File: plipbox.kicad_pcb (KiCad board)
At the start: 2 copper layers, 10 parts, among them P1 PWR, P2 PARALLEL_PORT, P3 RS232, U1 MAX3221, U2 ARDUINO_NANO_V3

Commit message: Routing
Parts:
- moved C2 5.93 mm to (181.2, 120.2), turned to 180 degrees
- moved P3 3.43 mm to (172.5, 120.5), turned to 180 degrees
- moved P1 2.12 mm to (172.5, 104.0)
- moved C3 1.68 mm to (181.2, 107.5), turned to 0 degrees
- moved C1 1.46 mm to (181.2, 109.8), turned to 180 degrees
- moved C4 0.56 mm to (178.2, 108.5)
- moved C5 0.25 mm to (176.0, 114.8)
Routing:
- net Net-(C4-Pad1): track 0.00 -> 5.49 mm
- net Net-(C4-Pad2): track 0.00 -> 2.92 mm
- net Net-(C1-Pad1): track 0.00 -> 2.54 mm
- net Net-(C1-Pad2): track 0.00 -> 2.31 mm
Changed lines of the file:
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@@
     (thickness 1.6)
     (drawings 1)
-    (tracks 67)
+    (tracks 79)
     (zones 0)
     (modules 10)
@@
   )
   (setup
-    (last_trace_width 0.3)
+    (last_trace_width 0.25)
     (user_trace_width 0.3)
     (user_trace_width 0.5)
@@
   )
   (module Capacitors_SMD:C_0603_HandSoldering (layer F.Cu)
-    (at 180 109 90)
+    (at 181.25 109.75 180)
     (descr "Capacitor SMD 0603, hand soldering")
     (tags "capacitor 0603")
     (attr smd)
-    (fp_text reference C1 (at 0 -1.25 90) (layer F.SilkS)
-      (effects (font (size 1 1) (thickness 0.15)))
-    )
-    (fp_text value 47n (at 0 1.5 90) (layer F.Fab)
-      (effects (font (size 1 1) (thickness 0.15)))
-    )
-    (fp_text user %R (at 0 -1.25 90) (layer F.Fab)
+    (fp_text reference C1 (at 0 -1.25 180) (layer F.SilkS)
+      (effects (font (size 1 1) (thickness 0.15)))
+    )
+    (fp_text value 47n (at 0 1.5 180) (layer F.Fab)
+      (effects (font (size 1 1) (thickness 0.15)))
+    )
+    (fp_text user %R (at 0 -1.25 180) (layer F.Fab)
       (effects (font (size 1 1) (thickness 0.15)))
     )
@@
     (fp_line (start 1.8 0.65) (end 1.8 -0.65) (layer F.CrtYd) (width 0.05))
     (fp_line (start 1.8 0.65) (end -1.8 0.65) (layer F.CrtYd) (width 0.05))
-    (pad 1 smd rect (at -0.95 0 90) (size 1.2 0.75) (layers F.Cu F.Paste F.Mask)
+    (pad 1 smd rect (at -0.95 0 180) (size 1.2 0.75) (layers F.Cu F.Paste F.Mask)
       (net 1 "Net-(C1-Pad1)"))
-    (pad 2 smd rect (at 0.95 0 90) (size 1.2 0.75) (layers F.Cu F.Paste F.Mask)
+    (pad 2 smd rect (at 0.95 0 180) (size 1.2 0.75) (layers F.Cu F.Paste F.Mask)
       (net 2 "Net-(C1-Pad2)"))
     (model Capacitors_SMD.3dshapes/C_0603.wrl
@@
   )
   (module Capacitors_SMD:C_0603_HandSoldering (layer F.Cu)
-    (at 184 115 90)
+    (at 181.25 120.25 180)
     (descr "Capacitor SMD 0603, hand soldering")
     (tags "capacitor 0603")
     (attr smd)
-    (fp_text reference C2 (at 0 -1.25 90) (layer F.SilkS)
-      (effects (font (size 1 1) (thickness 0.15)))
-    )
-    (fp_text value 100n (at 0 1.5 90) (layer F.Fab)
-      (effects (font (size 1 1) (thickness 0.15)))
-    )
-    (fp_text user %R (at 0 -1.25 90) (layer F.Fab)
+    (fp_text reference C2 (at 0 -1.25 180) (layer F.SilkS)
+      (effects (font (size 1 1) (thickness 0.15)))
+    )
+    (fp_text value 100n (at 0 1.5 180) (layer F.Fab)
+      (effects (font (size 1 1) (thickness 0.15)))
+    )
+    (fp_text user %R (at 0 -1.25 180) (layer F.Fab)
       (effects (font (size 1 1) (thickness 0.15)))
     )
@@
     (fp_line (start 1.8 0.65) (end 1.8 -0.65) (layer F.CrtYd) (width 0.05))
     (fp_line (start 1.8 0.65) (end -1.8 0.65) (layer F.CrtYd) (width 0.05))
-    (pad 1 smd rect (at -0.95 0 90) (size 1.2 0.75) (layers F.Cu F.Paste F.Mask)
+    (pad 1 smd rect (at -0.95 0 180) (size 1.2 0.75) (layers F.Cu F.Paste F.Mask)
       (net 3 /+5V))
-    (pad 2 smd rect (at 0.95 0 90) (size 1.2 0.75) (layers F.Cu F.Paste F.Mask)
+    (pad 2 smd rect (at 0.95 0 180) (size 1.2 0.75) (layers F.Cu F.Paste F.Mask)
       (net 4 GND))
     (model Capacitors_SMD.3dshapes/C_0603.wrl
@@
   )
   (module Capacitors_SMD:C_0603_HandSoldering (layer F.Cu)
-    (at 182 109 90)
+    (at 181.25 107.5)
     (descr "Capacitor SMD 0603, hand soldering")
     (tags "capacitor 0603")
     (attr smd)
-    (fp_text reference C3 (at 0 -1.25 90) (layer F.SilkS)
-      (effects (font (size 1 1) (thickness 0.15)))
-    )
-    (fp_text value 330n (at 0 1.5 90) (layer F.Fab)
-      (effects (font (size 1 1) (thickness 0.15)))
-    )
-    (fp_text user %R (at 0 -1.25 90) (layer F.Fab)
+    (fp_text reference C3 (at 0 -1.25) (layer F.SilkS)
+      (effects (font (size 1 1) (thickness 0.15)))
+    )
+    (fp_text value 330n (at 0 1.5) (layer F.Fab)
+      (effects (font (size 1 1) (thickness 0.15)))
+    )
+    (fp_text user %R (at 0 -1.25) (layer F.Fab)
       (effects (font (size 1 1) (thickness 0.15)))
     )
@@
     (fp_line (start 1.8 0.65) (end 1.8 -0.65) (layer F.CrtYd) (width 0.05))
     (fp_line (start 1.8 0.65) (end -1.8 0.65) (layer F.CrtYd) (width 0.05))
-    (pad 1 smd rect (at -0.95 0 90) (size 1.2 0.75) (layers F.Cu F.Paste F.Mask)
+    (pad 1 smd rect (at -0.95 0) (size 1.2 0.75) (layers F.Cu F.Paste F.Mask)
       (net 5 "Net-(C3-Pad1)"))
-    (pad 2 smd rect (at 0.95 0 90) (size 1.2 0.75) (layers F.Cu F.Paste F.Mask)
+    (pad 2 smd rect (at 0.95 0) (size 1.2 0.75) (layers F.Cu F.Paste F.Mask)
       (net 4 GND))
     (model Capacitors_SMD.3dshapes/C_0603.wrl
@@
   )
   (module Capacitors_SMD:C_0603_HandSoldering (layer F.Cu)
-    (at 178 109 270)
+    (at 178.25 108.5 270)
     (descr "Capacitor SMD 0603, hand soldering")
     (tags "capacitor 0603")
@@
   )
   (module Capacitors_SMD:C_0603_HandSoldering (layer F.Cu)
-    (at 176 115 270)
+    (at 176 114.75 270)
     (descr "Capacitor SMD 0603, hand soldering")
     (tags "capacitor 0603")
@@
   )
   (module Pin_Headers:Pin_Header_Straight_1x03_Pitch2.54mm (layer F.Cu)
-    (at 171 105.46)
+    (at 172.5 103.96)
     (descr "Through hole straight pin header, 1x03, 2.54mm pitch, single row")
     (tags "Through hole pin header THT 1x03 2.54mm single row")
@@
   )
   (module Pin_Headers:Pin_Header_Straight_1x03_Pitch2.54mm (layer F.Cu)
-    (at 171 117.46)
+    (at 172.5 120.54 180)
     (descr "Through hole straight pin header, 1x03, 2.54mm pitch, single row")
     (tags "Through hole pin header THT 1x03 2.54mm single row")
-    (fp_text reference P3 (at 0 -2.33) (layer F.SilkS)
-      (effects (font (size 1 1) (thickness 0.15)))
-    )
-    (fp_text value RS232 (at 0 7.41) (layer F.Fab)
+    (fp_text reference P3 (at 0 -2.33 180) (layer F.SilkS)
+      (effects (font (size 1 1) (thickness 0.15)))
+    )
+    (fp_text value RS232 (at 0 7.41 180) (layer F.Fab)
       (effects (font (size 1 1) (thickness 0.15)))
     )
@@
     (fp_line (start 1.8 6.85) (end 1.8 -1.8) (layer F.CrtYd) (width 0.05))
     (fp_line (start 1.8 -1.8) (end -1.8 -1.8) (layer F.CrtYd) (width 0.05))
-    (fp_text user %R (at 0 -2.33) (layer F.Fab)
-      (effects (font (size 1 1) (thickness 0.15)))
-    )
-    (pad 1 thru_hole rect (at 0 0) (size 1.7 1.7) (drill 1) (layers *.Cu *.Mask)
+    (fp_text user %R (at 0 -2.33 180) (layer F.Fab)
+      (effects (font (size 1 1) (thickness 0.15)))
+    )
+    (pad 1 thru_hole rect (at 0 0 180) (size 1.7 1.7) (drill 1) (layers *.Cu *.Mask)
       (net 23 /DOUT))
-    (pad 2 thru_hole oval (at 0 2.54) (size 1.7 1.7) (drill 1) (layers *.Cu *.Mask)
+    (pad 2 thru_hole oval (at 0 2.54 180) (size 1.7 1.7) (drill 1) (layers *.Cu *.Mask)
       (net 24 /RIN))
-    (pad 3 thru_hole oval (at 0 5.08) (size 1.7 1.7) (drill 1) (layers *.Cu *.Mask)
+    (pad 3 thru_hole oval (at 0 5.08 180) (size 1.7 1.7) (drill 1) (layers *.Cu *.Mask)
       (net 4 GND))
     (model ${KISYS3DMOD}/Pin_Headers.3dshapes/Pin_Header_Straight_1x03_Pitch2.54mm.wrl
@@
     (arrow2b (pts (xy 245 80) (xy 245.586421 81.126504)))
   )
+  (segment (start 181.625 112.05) (end 181.625 110.325) (width 0.3) (layer F.Cu) (net 1))
+  (segment (start 181.625 110.325) (end 182.2 109.75) (width 0.3) (layer F.Cu) (net 1))
+  (segment (start 180.325 112.05) (end 180.325 109.775) (width 0.3) (layer F.Cu) (net 2))
+  (segment (start 180.325 109.775) (end 180.3 109.75) (width 0.3) (layer F.Cu) (net 2))
+  (segment (start 179.25 110.5) (end 179.675 110.925) (width 0.3) (layer F.Cu) (net 6))
+  (segment (start 179.675 110.925) (end 179.675 112.05) (width 0.3) (layer F.Cu) (net 6))
+  (segment (start 179.25 107.875) (end 179.25 110.5) (width 0.3) (layer F.Cu) (net 6))
+  (segment (start 178.25 107.55) (end 178.925 107.55) (width 0.3) (layer F.Cu) (net 6))
+  (segment (start 178.925 107.55) (end 179.25 107.875) (width 0.3) (layer F.Cu) (net 6))
+  (segment (start 178.25 109.45) (end 178.25 110.35) (width 0.3) (layer F.Cu) (net 7))
+  (segment (start 178.25 110.35) (end 179.025 111.125) (width 0.3) (layer F.Cu) (net 7))
+  (segment (start 179.025 111.125) (end 179.025 112.05) (width 0.3) (layer F.Cu) (net 7))
   (segment (start 214.235 97.84) (end 214.235 99.042081) (width 0.3) (layer F.Cu) (net 10))
   (segment (start 216.5 123) (end 201.82 123) (width 0.3) (layer F.Cu) (net 10))

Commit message: Board outline
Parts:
- moved C3 6.39 mm to (184.5, 113.0), turned to 90 degrees
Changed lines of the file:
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@@
     (area 0 0 0 0)
     (thickness 1.6)
-    (drawings 1)
+    (drawings 10)
     (tracks 79)
     (zones 0)
@@
     (pad_to_mask_clearance 0.2)
     (aux_axis_origin 0 0)
-    (visible_elements FFFFFF7F)
+    (visible_elements FFFEFF7F)
     (pcbplotparams
       (layerselection 0x00030_80000001)
@@
   )
   (module Capacitors_SMD:C_0603_HandSoldering (layer F.Cu)
-    (at 181.25 107.5)
+    (at 184.5 113 90)
     (descr "Capacitor SMD 0603, hand soldering")
     (tags "capacitor 0603")
     (attr smd)
-    (fp_text reference C3 (at 0 -1.25) (layer F.SilkS)
-      (effects (font (size 1 1) (thickness 0.15)))
-    )
-    (fp_text value 330n (at 0 1.5) (layer F.Fab)
-      (effects (font (size 1 1) (thickness 0.15)))
-    )
-    (fp_text user %R (at 0 -1.25) (layer F.Fab)
+    (fp_text reference C3 (at 0 -1.25 90) (layer F.SilkS)
+      (effects (font (size 1 1) (thickness 0.15)))
+    )
+    (fp_text value 330n (at 0 1.5 90) (layer F.Fab)
+      (effects (font (size 1 1) (thickness 0.15)))
+    )
+    (fp_text user %R (at 0 -1.25 90) (layer F.Fab)
       (effects (font (size 1 1) (thickness 0.15)))
     )
@@
     (fp_line (start 1.8 0.65) (end 1.8 -0.65) (layer F.CrtYd) (width 0.05))
     (fp_line (start 1.8 0.65) (end -1.8 0.65) (layer F.CrtYd) (width 0.05))
-    (pad 1 smd rect (at -0.95 0) (size 1.2 0.75) (layers F.Cu F.Paste F.Mask)
+    (pad 1 smd rect (at -0.95 0 90) (size 1.2 0.75) (layers F.Cu F.Paste F.Mask)
       (net 5 "Net-(C3-Pad1)"))
-    (pad 2 smd rect (at 0.95 0) (size 1.2 0.75) (layers F.Cu F.Paste F.Mask)
+    (pad 2 smd rect (at 0.95 0 90) (size 1.2 0.75) (layers F.Cu F.Paste F.Mask)
       (net 4 GND))
     (model Capacitors_SMD.3dshapes/C_0603.wrl
@@
     )
   )
+  (gr_line (start 224 87.5) (end 171.5 87.5) (layer Margin) (width 0.2))
+  (gr_arc (start 224 90) (end 224 87.5) (angle 90) (layer Margin) (width 0.2))
+  (gr_arc (start 171.5 90) (end 169 90) (angle 90) (layer Margin) (width 0.2))
+  (gr_arc (start 171.5 121.5) (end 171.5 124) (angle 90) (layer Margin) (width 0.2))
+  (gr_arc (start 224 121.5) (end 226.5 121.5) (angle 90) (layer Margin) (width 0.2))
+  (dimension 59.5 (width 0.3) (layer Cmts.User)
+    (gr_text "59.500 mm" (at 197.75 129.35) (layer Cmts.User)
+      (effects (font (size 1.5 1.5) (thickness 0.3)))
+    )
+    (feature1 (pts (xy 227.5 125) (xy 227.5 130.7)))
+    (feature2 (pts (xy 168 125) (xy 168 130.7)))
+    (crossbar (pts (xy 168 128) (xy 227.5 128)))
+    (arrow1a (pts (xy 227.5 128) (xy 226.373496 128.586421)))
+    (arrow1b (pts (xy 227.5 128) (xy 226.373496 127.413579)))
+    (arrow2a (pts (xy 168 128) (xy 169.126504 128.586421)))
+    (arrow2b (pts (xy 168 128) (xy 169.126504 127.413579)))
+  )
+  (gr_line (start 226.5 90) (end 226.5 121.5) (layer Margin) (width 0.2))
+  (gr_line (start 171.5 124) (end 224 124) (layer Margin) (width 0.2))
+  (gr_line (start 169 90) (end 169 121.5) (layer Margin) (width 0.2))
   (dimension 45 (width 0.3) (layer Cmts.User)
     (gr_text "45.000 mm" (at 246.35 102.5 270) (layer Cmts.User)

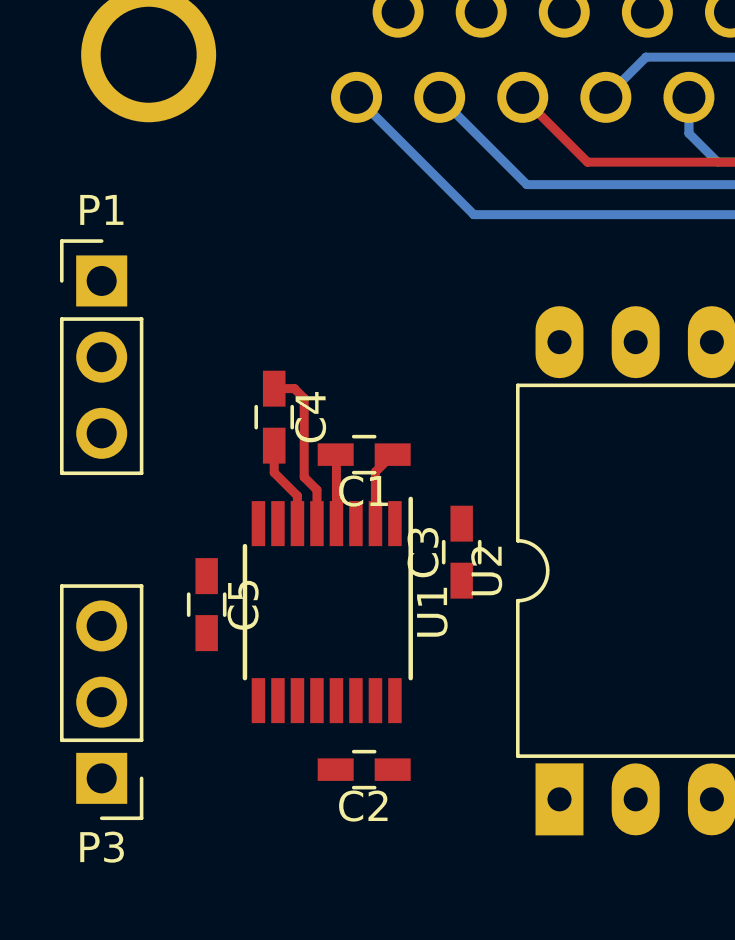
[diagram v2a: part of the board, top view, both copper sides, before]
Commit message: More compact U1
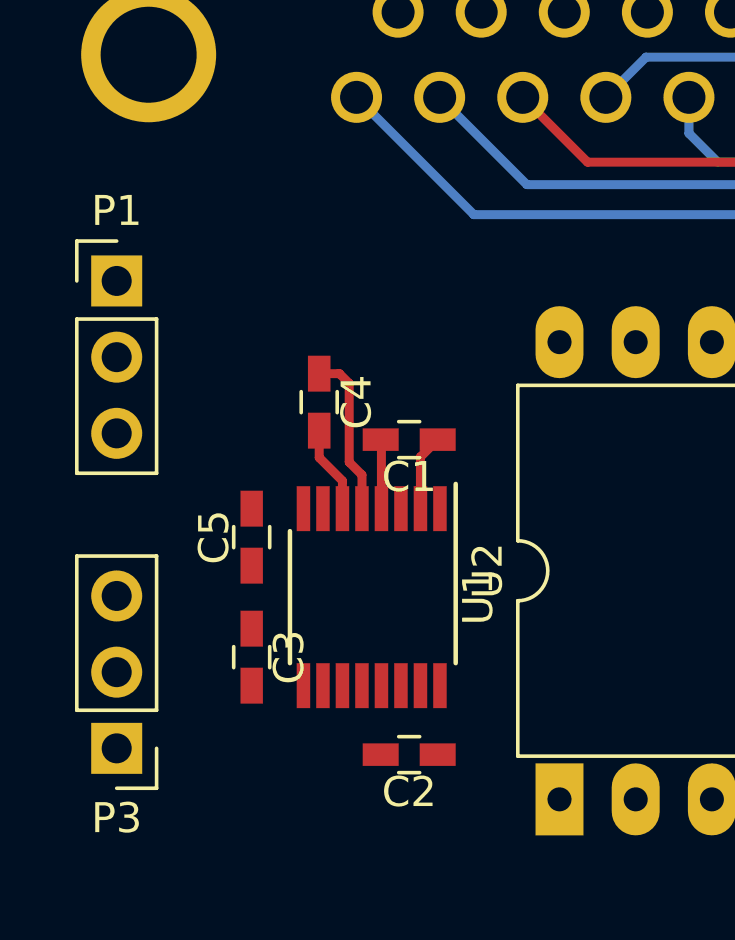
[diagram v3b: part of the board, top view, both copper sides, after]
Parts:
- moved C3 7.83 mm to (177.5, 116.5), turned to 270 degrees
- moved C5 2.70 mm to (177.5, 112.5), turned to 90 degrees
- moved C1 1.58 mm to (182.8, 109.2)
- moved C2 1.58 mm to (182.8, 119.8)
- moved C4 1.58 mm to (179.8, 108.0)
- moved U1 1.58 mm to (181.5, 114.5)
- moved P3 1.12 mm to (173.0, 119.5)
- moved P1 0.50 mm to (173.0, 104.0)
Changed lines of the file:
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@@
   )
   (setup
-    (last_trace_width 0.25)
+    (last_trace_width 0.3)
     (user_trace_width 0.3)
     (user_trace_width 0.5)
@@
   )
   (module Capacitors_SMD:C_0603_HandSoldering (layer F.Cu)
-    (at 181.25 109.75 180)
+    (at 182.75 109.25 180)
     (descr "Capacitor SMD 0603, hand soldering")
     (tags "capacitor 0603")
@@
   )
   (module Capacitors_SMD:C_0603_HandSoldering (layer F.Cu)
-    (at 181.25 120.25 180)
+    (at 182.75 119.75 180)
     (descr "Capacitor SMD 0603, hand soldering")
     (tags "capacitor 0603")
@@
   )
   (module Capacitors_SMD:C_0603_HandSoldering (layer F.Cu)
-    (at 184.5 113 90)
+    (at 177.5 116.5 270)
     (descr "Capacitor SMD 0603, hand soldering")
     (tags "capacitor 0603")
     (attr smd)
-    (fp_text reference C3 (at 0 -1.25 90) (layer F.SilkS)
-      (effects (font (size 1 1) (thickness 0.15)))
-    )
-    (fp_text value 330n (at 0 1.5 90) (layer F.Fab)
-      (effects (font (size 1 1) (thickness 0.15)))
-    )
-    (fp_text user %R (at 0 -1.25 90) (layer F.Fab)
+    (fp_text reference C3 (at 0 -1.25 270) (layer F.SilkS)
+      (effects (font (size 1 1) (thickness 0.15)))
+    )
+    (fp_text value 330n (at 0 1.5 270) (layer F.Fab)
+      (effects (font (size 1 1) (thickness 0.15)))
+    )
+    (fp_text user %R (at 0 -1.25 270) (layer F.Fab)
       (effects (font (size 1 1) (thickness 0.15)))
     )
@@
     (fp_line (start 1.8 0.65) (end 1.8 -0.65) (layer F.CrtYd) (width 0.05))
     (fp_line (start 1.8 0.65) (end -1.8 0.65) (layer F.CrtYd) (width 0.05))
-    (pad 1 smd rect (at -0.95 0 90) (size 1.2 0.75) (layers F.Cu F.Paste F.Mask)
+    (pad 1 smd rect (at -0.95 0 270) (size 1.2 0.75) (layers F.Cu F.Paste F.Mask)
       (net 5 "Net-(C3-Pad1)"))
-    (pad 2 smd rect (at 0.95 0 90) (size 1.2 0.75) (layers F.Cu F.Paste F.Mask)
+    (pad 2 smd rect (at 0.95 0 270) (size 1.2 0.75) (layers F.Cu F.Paste F.Mask)
       (net 4 GND))
     (model Capacitors_SMD.3dshapes/C_0603.wrl
@@
   )
   (module Capacitors_SMD:C_0603_HandSoldering (layer F.Cu)
-    (at 178.25 108.5 270)
+    (at 179.75 108 270)
     (descr "Capacitor SMD 0603, hand soldering")
     (tags "capacitor 0603")
@@
   )
   (module Capacitors_SMD:C_0603_HandSoldering (layer F.Cu)
-    (at 176 114.75 270)
+    (at 177.5 112.5 90)
     (descr "Capacitor SMD 0603, hand soldering")
     (tags "capacitor 0603")
     (attr smd)
-    (fp_text reference C5 (at 0 -1.25 270) (layer F.SilkS)
-      (effects (font (size 1 1) (thickness 0.15)))
-    )
-    (fp_text value 330n (at 0 1.5 270) (layer F.Fab)
-      (effects (font (size 1 1) (thickness 0.15)))
-    )
-    (fp_text user %R (at 0 -1.25 270) (layer F.Fab)
+    (fp_text reference C5 (at 0 -1.25 90) (layer F.SilkS)
+      (effects (font (size 1 1) (thickness 0.15)))
+    )
+    (fp_text value 330n (at 0 1.5 90) (layer F.Fab)
+      (effects (font (size 1 1) (thickness 0.15)))
+    )
+    (fp_text user %R (at 0 -1.25 90) (layer F.Fab)
       (effects (font (size 1 1) (thickness 0.15)))
     )
@@
     (fp_line (start 1.8 0.65) (end 1.8 -0.65) (layer F.CrtYd) (width 0.05))
     (fp_line (start 1.8 0.65) (end -1.8 0.65) (layer F.CrtYd) (width 0.05))
-    (pad 1 smd rect (at -0.95 0 270) (size 1.2 0.75) (layers F.Cu F.Paste F.Mask)
+    (pad 1 smd rect (at -0.95 0 90) (size 1.2 0.75) (layers F.Cu F.Paste F.Mask)
       (net 8 "Net-(C5-Pad1)"))
-    (pad 2 smd rect (at 0.95 0 270) (size 1.2 0.75) (layers F.Cu F.Paste F.Mask)
+    (pad 2 smd rect (at 0.95 0 90) (size 1.2 0.75) (layers F.Cu F.Paste F.Mask)
       (net 4 GND))
     (model Capacitors_SMD.3dshapes/C_0603.wrl
@@
   )
   (module Pin_Headers:Pin_Header_Straight_1x03_Pitch2.54mm (layer F.Cu)
-    (at 172.5 103.96)
+    (at 173 103.96)
     (descr "Through hole straight pin header, 1x03, 2.54mm pitch, single row")
     (tags "Through hole pin header THT 1x03 2.54mm single row")
@@
   )
   (module Pin_Headers:Pin_Header_Straight_1x03_Pitch2.54mm (layer F.Cu)
-    (at 172.5 120.54 180)
+    (at 173 119.54 180)
     (descr "Through hole straight pin header, 1x03, 2.54mm pitch, single row")
     (tags "Through hole pin header THT 1x03 2.54mm single row")
@@
   )
   (module Housings_SSOP:TSSOP-16_4.4x5mm_Pitch0.65mm (layer F.Cu)
-    (at 180 115 270)
+    (at 181.5 114.5 270)
     (descr "16-Lead Plastic Thin Shrink Small Outline (ST)-4.4 mm Body [TSSOP] (see Microchip Packaging Specification 00000049BS.pdf)")
     (tags "SSOP 0.65")
@@
     (arrow2b (pts (xy 245 80) (xy 245.586421 81.126504)))
   )
-  (segment (start 181.625 112.05) (end 181.625 110.325) (width 0.3) (layer F.Cu) (net 1))
-  (segment (start 181.625 110.325) (end 182.2 109.75) (width 0.3) (layer F.Cu) (net 1))
-  (segment (start 180.325 112.05) (end 180.325 109.775) (width 0.3) (layer F.Cu) (net 2))
-  (segment (start 180.325 109.775) (end 180.3 109.75) (width 0.3) (layer F.Cu) (net 2))
-  (segment (start 179.25 110.5) (end 179.675 110.925) (width 0.3) (layer F.Cu) (net 6))
-  (segment (start 179.675 110.925) (end 179.675 112.05) (width 0.3) (layer F.Cu) (net 6))
-  (segment (start 179.25 107.875) (end 179.25 110.5) (width 0.3) (layer F.Cu) (net 6))
-  (segment (start 178.25 107.55) (end 178.925 107.55) (width 0.3) (layer F.Cu) (net 6))
-  (segment (start 178.925 107.55) (end 179.25 107.875) (width 0.3) (layer F.Cu) (net 6))
-  (segment (start 178.25 109.45) (end 178.25 110.35) (width 0.3) (layer F.Cu) (net 7))
-  (segment (start 178.25 110.35) (end 179.025 111.125) (width 0.3) (layer F.Cu) (net 7))
-  (segment (start 179.025 111.125) (end 179.025 112.05) (width 0.3) (layer F.Cu) (net 7))
+  (segment (start 183.125 111.55) (end 183.125 109.825) (width 0.3) (layer F.Cu) (net 1))
+  (segment (start 183.125 109.825) (end 183.7 109.25) (width 0.3) (layer F.Cu) (net 1))
+  (segment (start 181.825 111.55) (end 181.825 109.275) (width 0.3) (layer F.Cu) (net 2))
+  (segment (start 181.825 109.275) (end 181.8 109.25) (width 0.3) (layer F.Cu) (net 2))
+  (segment (start 180.75 110) (end 181.175 110.425) (width 0.3) (layer F.Cu) (net 6))
+  (segment (start 181.175 110.425) (end 181.175 111.55) (width 0.3) (layer F.Cu) (net 6))
+  (segment (start 180.75 107.375) (end 180.75 110) (width 0.3) (layer F.Cu) (net 6))
+  (segment (start 179.75 107.05) (end 180.425 107.05) (width 0.3) (layer F.Cu) (net 6))
+  (segment (start 180.425 107.05) (end 180.75 107.375) (width 0.3) (layer F.Cu) (net 6))
+  (segment (start 179.75 108.95) (end 179.75 109.85) (width 0.3) (layer F.Cu) (net 7))
+  (segment (start 179.75 109.85) (end 180.525 110.625) (width 0.3) (layer F.Cu) (net 7))
+  (segment (start 180.525 110.625) (end 180.525 111.55) (width 0.3) (layer F.Cu) (net 7))
   (segment (start 214.235 97.84) (end 214.235 99.042081) (width 0.3) (layer F.Cu) (net 10))
   (segment (start 216.5 123) (end 201.82 123) (width 0.3) (layer F.Cu) (net 10))

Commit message: Routing
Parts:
- moved C1 1.80 mm to (181.8, 107.8)
- moved C2 1.80 mm to (181.8, 118.2)
- moved C3 1.80 mm to (176.5, 115.0)
- moved C4 1.80 mm to (178.8, 106.5)
- moved C5 1.80 mm to (176.5, 111.0)
- moved U1 1.80 mm to (180.5, 113.0)
- moved U2 1.54 mm to (186.2, 121.2)
- moved P2 0.12 mm to (197.5, 96.4)
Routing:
- net /+5V: track 0.00 -> 43.2 mm
- net /VIN: track 0.00 -> 15.9 mm
- net /RIN: track 0.00 -> 13.4 mm
- net /DOUT: track 0.00 -> 9.93 mm
- net Net-(C3-Pad1): track 0.00 -> 7.25 mm
- net /~ACK: track 45.4 -> 41.4 mm, vias 0 -> 1
- net /~STROBE: track 43.5 -> 47.3 mm
- net Net-(C5-Pad1): track 0.00 -> 3.78 mm
- net /BUSY: track 33.9 -> 31.2 mm, vias 0 -> 1
- net /SELECT: track 56.0 -> 58.6 mm
- net /DATA7: track 38.1 -> 36.6 mm, vias 0 -> 1
- net /POUT: track 38.9 -> 38.0 mm
- net /DATA4: track 10.3 -> 9.71 mm
- net /DATA3: track 10.2 -> 9.61 mm
- net /DATA6: track 28.9 -> 28.3 mm
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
